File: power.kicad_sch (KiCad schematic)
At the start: 21 parts, among them U1 AP62301_TSOT, U3 AP62301_TSOT

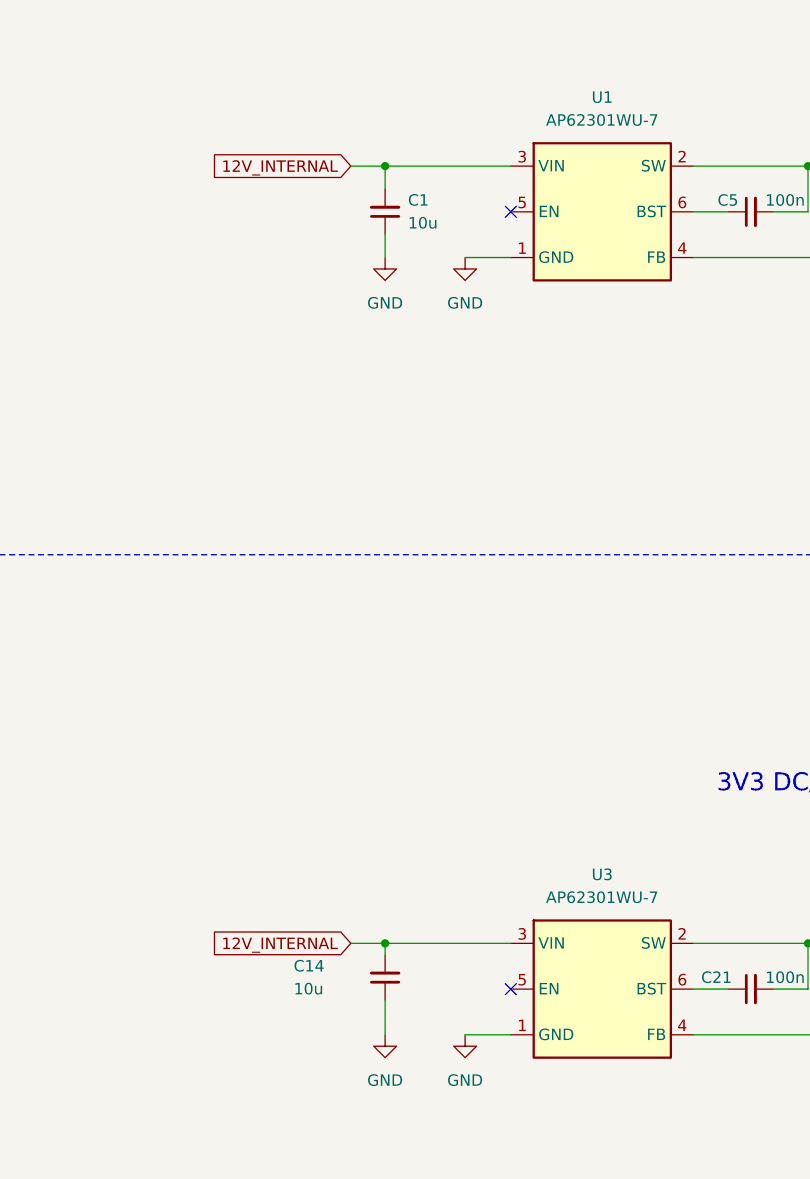
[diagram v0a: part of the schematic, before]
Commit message: [#62160] Add voltage divider on buck converter enable
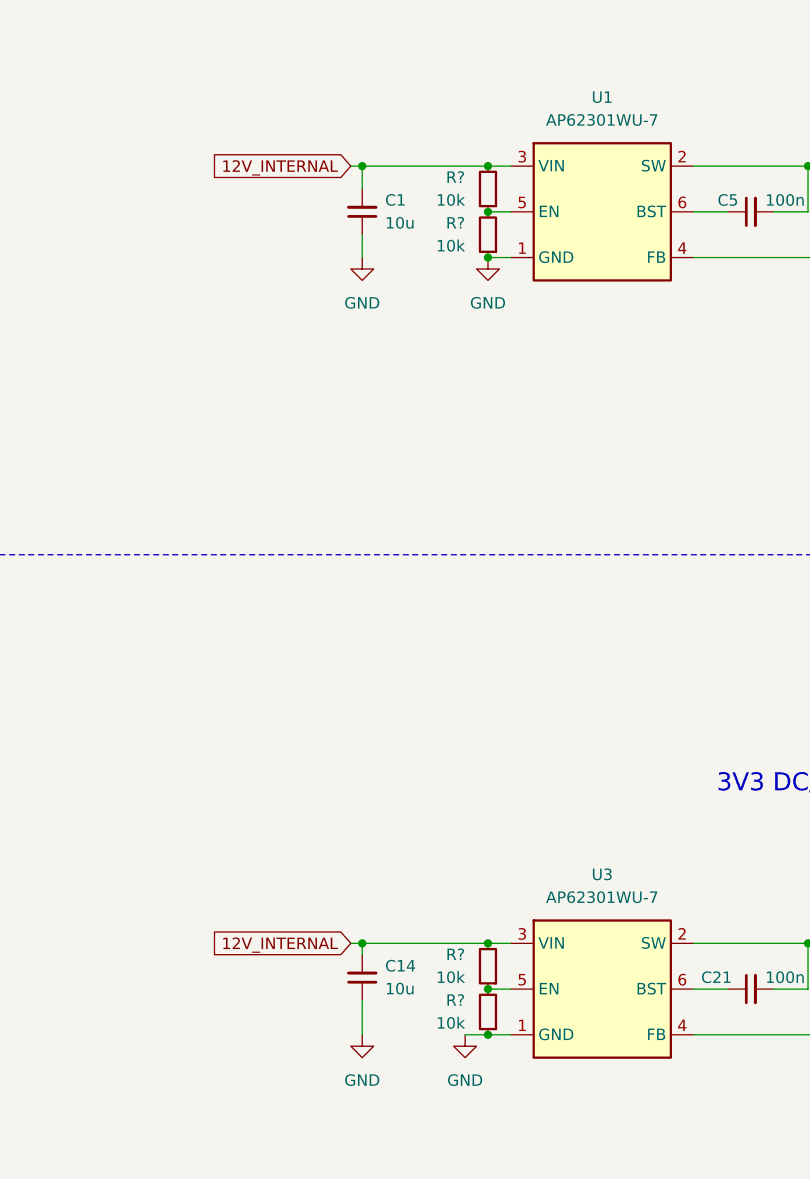
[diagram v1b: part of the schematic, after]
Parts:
- added R? (x4): R_10k_0402, antmicro-footprints:R_0402_1005Metric, symbol antmicroResistors0402:R_10k_0402
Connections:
- net 12V_INTERNAL: now also R?.2, R?.2
- net GND: now also R?.1, R?.1
- net at U3.5 (EN): now also R?.1, R?.2
- net at U1.5 (EN): now also R?.1, R?.2
- no-connect marks 2 -> 0
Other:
- moved on the sheet: C1, C14

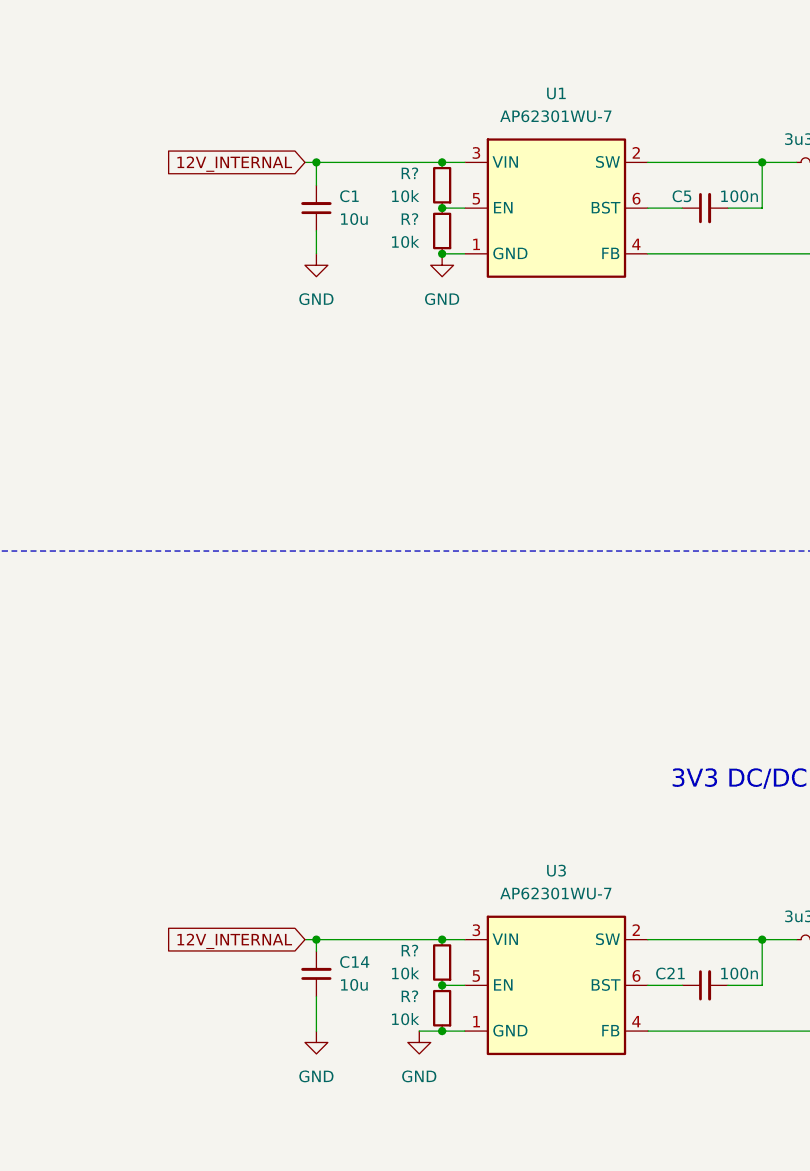
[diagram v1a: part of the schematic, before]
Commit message: [#62160] Add voltage divider on AP62301 enable
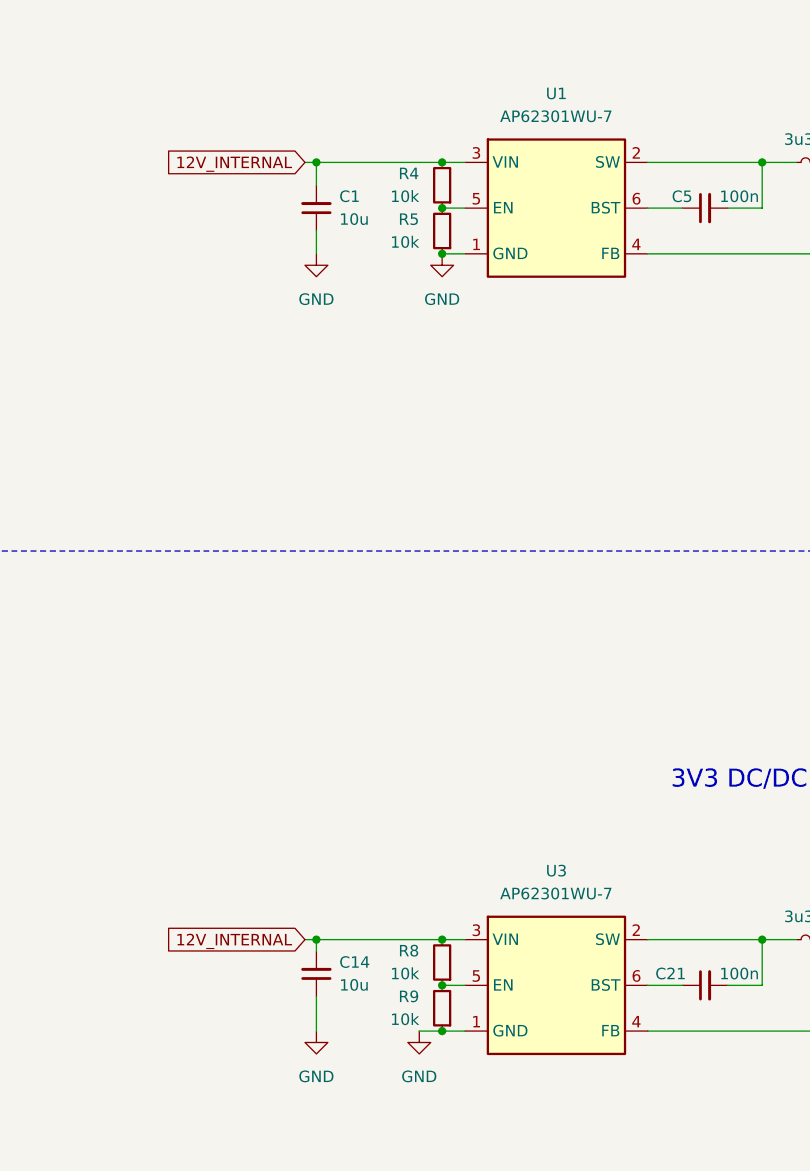
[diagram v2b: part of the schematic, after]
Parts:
- gave numbers to parts that had none: 4
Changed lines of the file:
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@@
   (symbol (lib_id "antmicroResistors0402:R_10k_0402") (at 165.1 182.88 270) (mirror x) (unit 1)
     (in_bom yes) (on_board yes) (dnp no)
-    (property "Reference" "R?" (at 162.56 179.07 90)
+    (property "Reference" "R8" (at 162.56 179.07 90)
       (effects (font (size 1.27 1.27) (thickness 0.15)) (justify right))
     )
@@
       (project "gpu-cluster-backplane"
         (path "/1dfa85fb-d2ca-4fb7-a43a-9f2dc5b08d74/00000000-0000-0000-0000-000062220f27"
-          (reference "R?") (unit 1)
+          (reference "R8") (unit 1)
         )
       )
@@
   (symbol (lib_id "antmicroResistors0402:R_10k_0402") (at 165.1 101.6 270) (mirror x) (unit 1)
     (in_bom yes) (on_board yes) (dnp no)
-    (property "Reference" "R?" (at 162.56 97.79 90)
+    (property "Reference" "R5" (at 162.56 97.79 90)
       (effects (font (size 1.27 1.27) (thickness 0.15)) (justify right))
     )
@@
       (project "gpu-cluster-backplane"
         (path "/1dfa85fb-d2ca-4fb7-a43a-9f2dc5b08d74/00000000-0000-0000-0000-000062220f27"
-          (reference "R?") (unit 1)
+          (reference "R5") (unit 1)
         )
       )
@@
   (symbol (lib_id "antmicroResistors0402:R_10k_0402") (at 165.1 187.96 270) (mirror x) (unit 1)
     (in_bom yes) (on_board yes) (dnp no)
-    (property "Reference" "R?" (at 162.56 184.15 90)
+    (property "Reference" "R9" (at 162.56 184.15 90)
       (effects (font (size 1.27 1.27) (thickness 0.15)) (justify right))
     )
@@
       (project "gpu-cluster-backplane"
         (path "/1dfa85fb-d2ca-4fb7-a43a-9f2dc5b08d74/00000000-0000-0000-0000-000062220f27"
-          (reference "R?") (unit 1)
+          (reference "R9") (unit 1)
         )
       )
@@
   (symbol (lib_id "antmicroResistors0402:R_10k_0402") (at 165.1 96.52 270) (mirror x) (unit 1)
     (in_bom yes) (on_board yes) (dnp no)
-    (property "Reference" "R?" (at 162.56 92.71 90)
+    (property "Reference" "R4" (at 162.56 92.71 90)
       (effects (font (size 1.27 1.27) (thickness 0.15)) (justify right))
     )
@@
       (project "gpu-cluster-backplane"
         (path "/1dfa85fb-d2ca-4fb7-a43a-9f2dc5b08d74/00000000-0000-0000-0000-000062220f27"
-          (reference "R?") (unit 1)
-        )
-      )
+          (reference "R4") (unit 1)
+        )
+      )
